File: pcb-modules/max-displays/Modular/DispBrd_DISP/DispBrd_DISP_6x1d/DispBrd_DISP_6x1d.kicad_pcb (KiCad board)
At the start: 2 copper layers, 45.7 x 23 mm, 9 parts, among them P8 Disp1x6

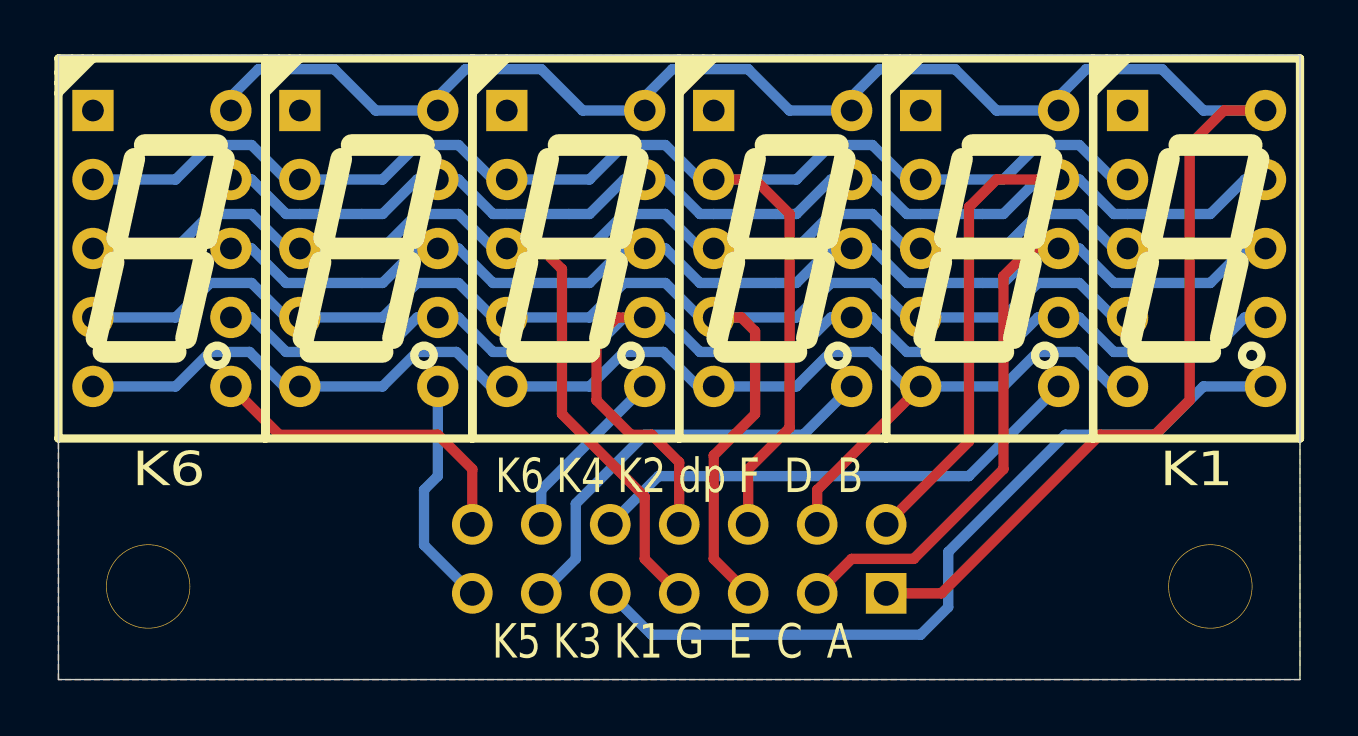
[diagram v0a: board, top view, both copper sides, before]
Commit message: Max Display panels, modular version FIX: Rear connector rotated 180deg on boards [3+2d], [3+3d], [6x1d] All boards: Silkscreen text on rear oriented correctly; board name added; Format update to KiCAD 6.0.6
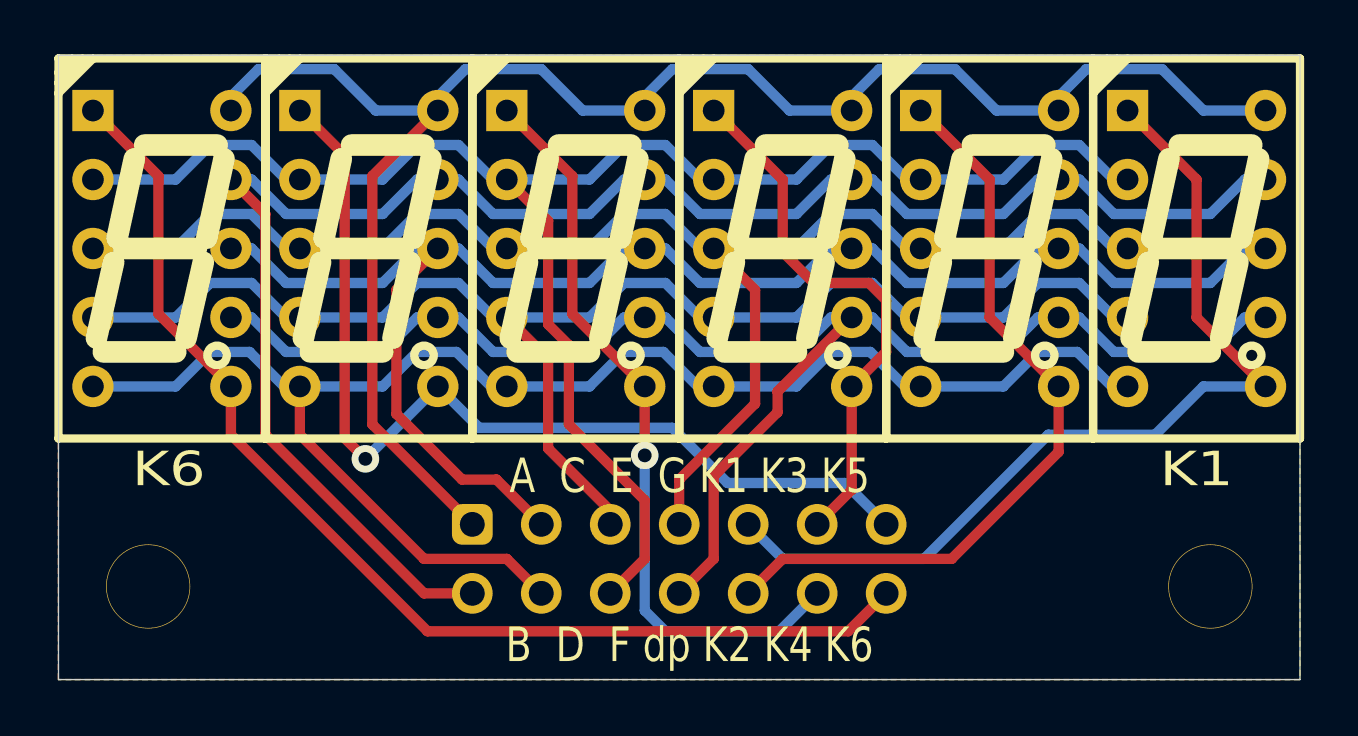
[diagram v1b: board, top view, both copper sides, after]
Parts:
- moved P8 15.5 mm to (53.6, 47.8), turned to -90 degrees
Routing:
- net /A5: track 12.2 -> 41.7 mm
- net /A4: track 8.57 -> 36.2 mm, vias 0 -> 1
- net /A3: track 6.66 -> 27.8 mm, vias 0 -> 1
- net /K_SegA: track 72.7 -> 61.1 mm
- net /K_SegG: track 62.2 -> 51.8 mm
- net /A1: track 18.6 -> 28.3 mm
- net /K_SegD: track 49.4 -> 55.9 mm
- net /A0: track 29.7 -> 34.5 mm
- net /K_SegC: track 61.7 -> 57.1 mm
- net /A2: track 15.8 -> 20.1 mm
- net /K_SegE: track 55.4 -> 51.5 mm
- net /K_SegB: track 60.0 -> 63.3 mm
- net /K_SegF: track 58.2 -> 60.7 mm
- net /K_SegDP: track 54.0 -> 56.2 mm
